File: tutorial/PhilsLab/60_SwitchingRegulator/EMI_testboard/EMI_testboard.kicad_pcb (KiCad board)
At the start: 2 copper layers, 11 parts

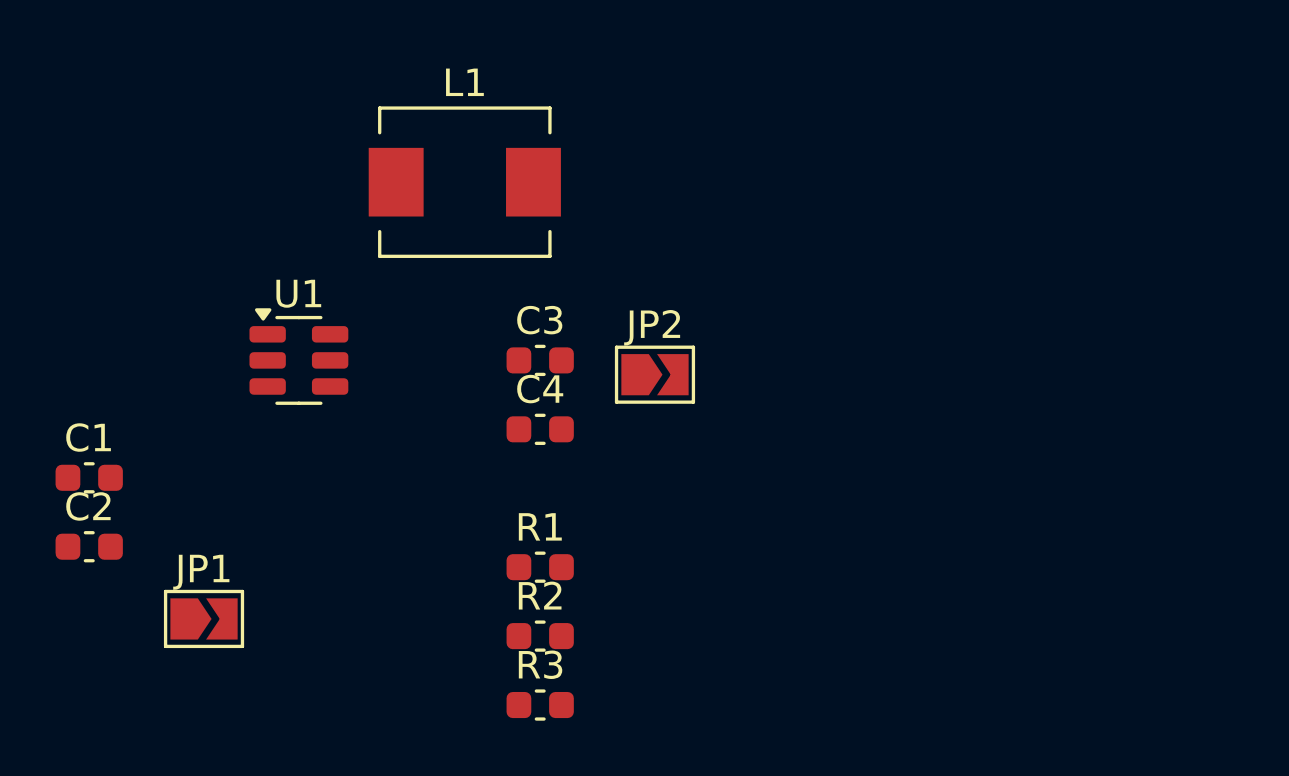
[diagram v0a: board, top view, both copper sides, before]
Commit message: Finished Buck converter from video #60
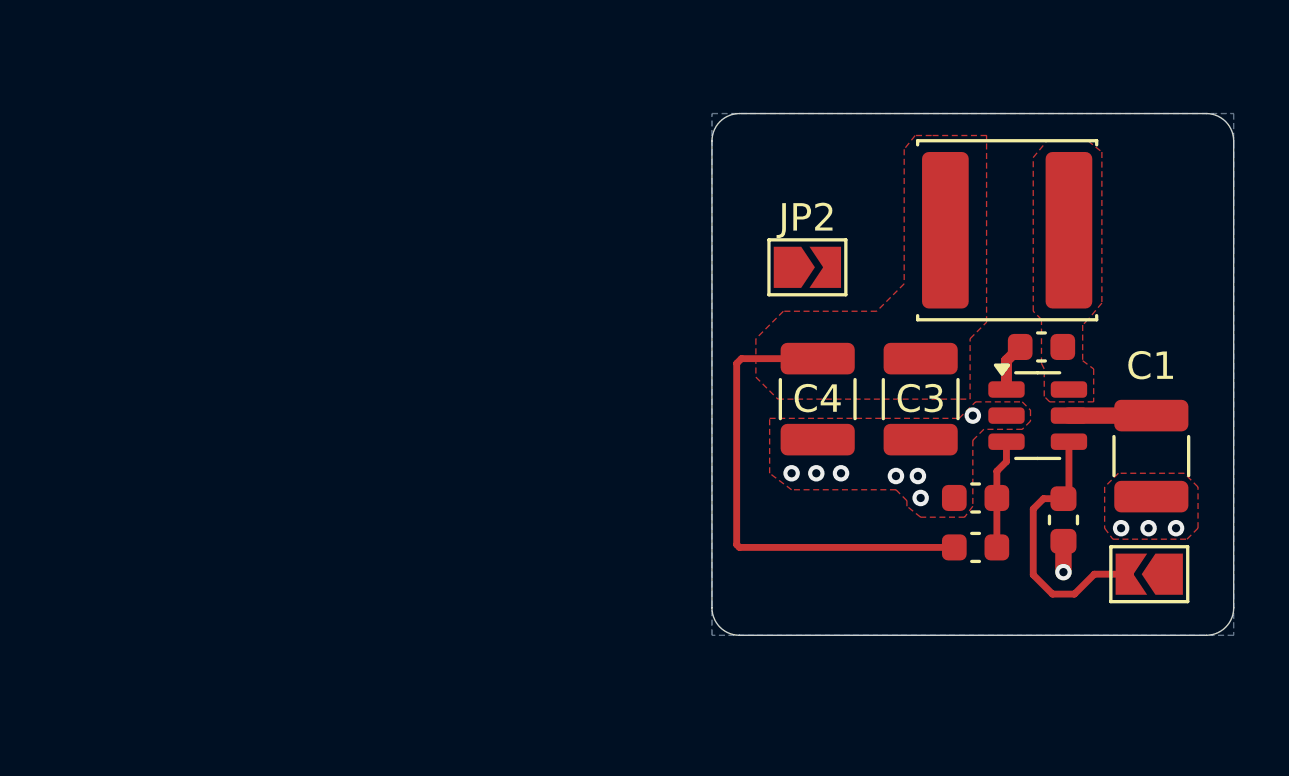
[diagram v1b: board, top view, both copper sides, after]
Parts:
- C1, C3, C4: footprint Capacitor_SMD:C_0603_1608Metric -> Capacitor_SMD:C_1210_3225Metric
- L1: footprint Inductor_SMD:L_Neosid_SM-PIC0512H -> Inductor_SMD:L_APV_ANR6045
- moved C1 38.7 mm to (110.0, 70.5), turned to -90 degrees
- moved C2 35.4 mm to (106.0, 66.5), turned to 180 degrees
- moved JP1 34.5 mm to (109.9, 74.8), turned to 180 degrees
- moved U1 27.0 mm to (105.9, 69.0)
- moved L1 19.8 mm to (104.8, 62.2), turned to 180 degrees
- moved R1 19.1 mm to (106.8, 72.8), turned to -90 degrees
- moved R3 16.9 mm to (103.6, 73.8), turned to 180 degrees
- moved R2 16.6 mm to (103.6, 72.0), turned to 180 degrees
- moved C3 13.9 mm to (101.6, 68.4), turned to -90 degrees
- moved C4 10.2 mm to (97.8, 68.4), turned to -90 degrees
- moved JP2 6.79 mm to (97.5, 63.6)
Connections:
- C3 pad 1: GND -> +3V3
- C3 pad 2: +3V3 -> GND
- C4 pad 1: GND -> +3V3
- C4 pad 2: +3V3 -> GND
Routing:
- net +3V3: track 0.00 -> 17.6 mm
- net Net-(JP1-B): track 0.00 -> 9.90 mm
- net Net-(U1-FB): track 0.00 -> 3.99 mm
- net VCC: track 0.00 -> 3.00 mm
- net Net-(U1-BST): track 0.00 -> 1.76 mm
- net GND: track 0.00 -> 1.12 mm, vias 0 -> 11
- added copper zone on F.Cu, net +3V3
- added copper zone on B.Cu, net GND
- added copper zone on F.Cu, net GND
- added copper zone on F.Cu, net Net-(U1-SW)
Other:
- board outline added: 19 x 19 mm

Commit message: VIDEO #3 :: finished schematic
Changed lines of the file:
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@@
 		(polygon
 			(pts
-				(xy 96.1 69.1) (xy 103 69.1) (xy 103.6 68.5) (xy 105.3 68.5) (xy 105.6 68.8) (xy 105.6 69.2) (xy 105.3 69.5)
-				(xy 103.9 69.5) (xy 103.5 69.9) (xy 103.5 72.3) (xy 103.2 72.7) (xy 101.6 72.7) (xy 101.1 72.3)
-				(xy 101.1 72.1) (xy 100.7 71.7) (xy 96.9 71.7) (xy 96.1 71.1)
+				(xy 96.1 69.1) (xy 103 69.1) (xy 103.73 68.37) (xy 105.43 68.37) (xy 105.72 68.66) (xy 105.72 69.25)
+				(xy 105.36 69.61) (xy 103.79 69.61) (xy 103.5 69.9) (xy 103.5 72.3) (xy 103.2 72.7) (xy 101.6 72.7)
+				(xy 101.1 72.3) (xy 101.1 72.1) (xy 100.7 71.7) (xy 96.9 71.7) (xy 96.1 71.1)
 			)
 		)
